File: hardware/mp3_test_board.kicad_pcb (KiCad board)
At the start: 2 copper layers, 113.1 x 53 mm, 128 parts, among them J1 874380343, J2 PJ-3270, J3 TF01-A, J4 532610371, P1 HRO-TYPE-C-31-M-12, SW1 TS-1010-C-A, SW2 TS-1157-X-F, SW3 TS-1157-X-F, SW4 TS-1157-X-F, SW5 TS-1157-X-F, SW6 TS-1157-X-F, SW7 TS-1010-C-A, SW8 TS-1010-C-A, U1 RT5750A, U10 OPA1652, U11 LM4562, U12 W25Q128JVSIQ, U13 XC6206P302MR, U2 RT9467, U3 RT4812, U4 F1C200S, U5 RT6150, U6 RT5750A, U7 RT5750A, U8 USBLC6-2SC6, U9 WM8741, Y1 Crystal_GND24

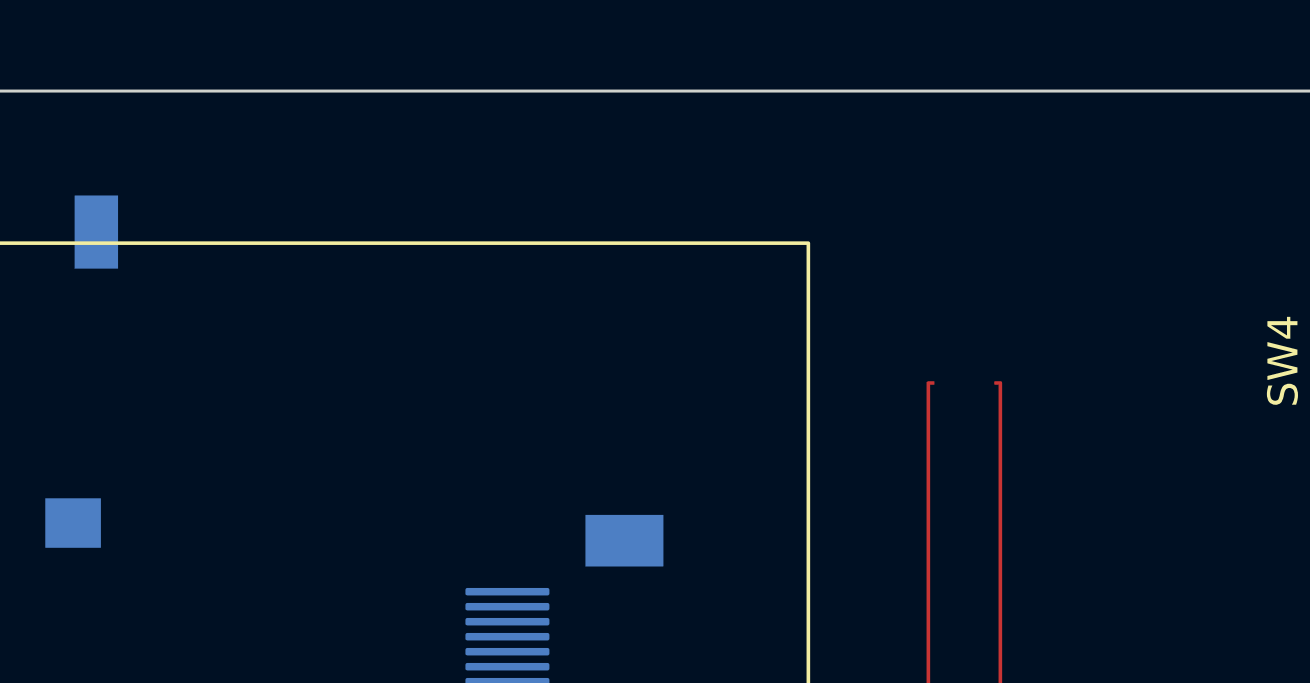
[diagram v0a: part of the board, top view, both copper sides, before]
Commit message: replaced dc-dc ics
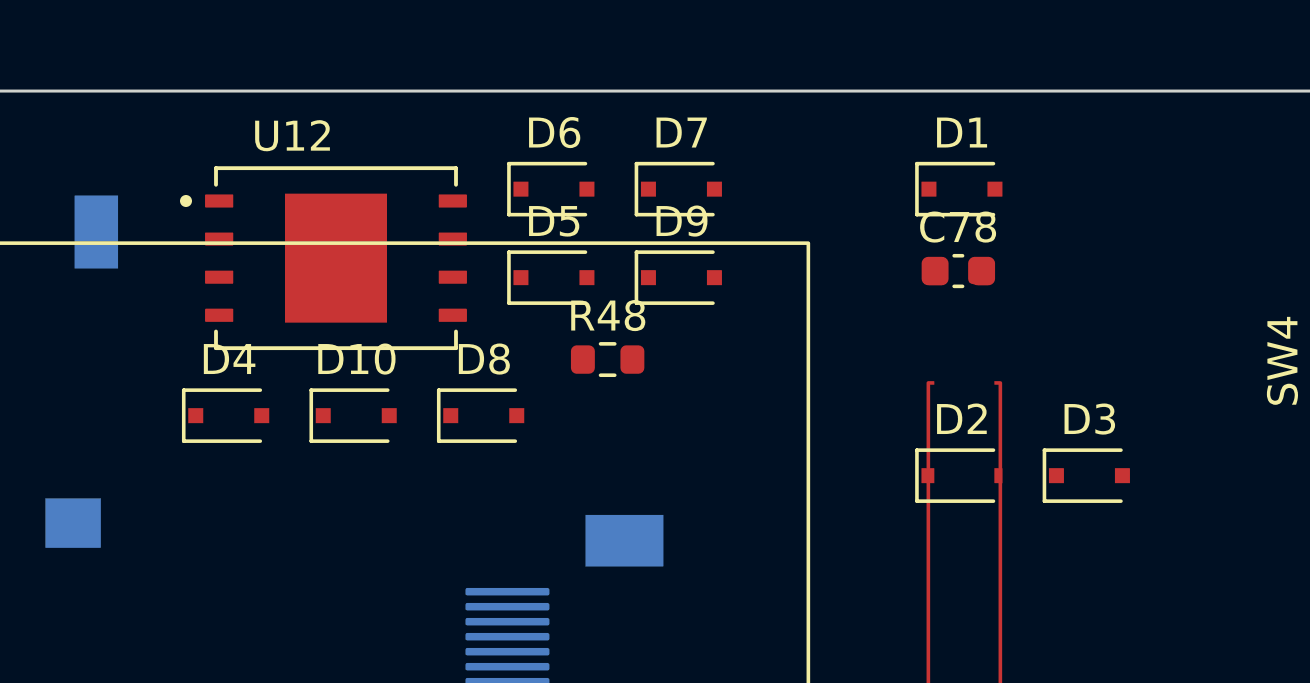
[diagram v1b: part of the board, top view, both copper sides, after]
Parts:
- added C78: C, rlib_passive:C_0603_1608Metric, F.Cu at (113.0, 64.0)
- added D1: PESD3V3L1BA, rlib_passive:D_SOD-323F, F.Cu at (113.1, 61.3)
- added D10: PESD3V3L1BA, rlib_passive:D_SOD-323F, F.Cu at (92.9, 68.8)
- added D2: PESD3V3L1BA, rlib_passive:D_SOD-323F, F.Cu at (113.1, 70.8)
- added D3: PESD3V3L1BA, rlib_passive:D_SOD-323F, F.Cu at (117.4, 70.8)
- added D4: PESD3V3L1BA, rlib_passive:D_SOD-323F, F.Cu at (88.7, 68.8)
- added D5: PESD3V3L1BA, rlib_passive:D_SOD-323F, F.Cu at (99.5, 64.2)
- added D6: PESD3V3L1BA, rlib_passive:D_SOD-323F, F.Cu at (99.5, 61.3)
- added D7: PESD3V3L1BA, rlib_passive:D_SOD-323F, F.Cu at (103.8, 61.3)
- added D8: PESD3V3L1BA, rlib_passive:D_SOD-323F, F.Cu at (97.2, 68.8)
- added D9: PESD3V3L1BA, rlib_passive:D_SOD-323F, F.Cu at (103.8, 64.2)
- added R48: R, rlib_passive:R_0603_1608Metric, F.Cu at (101.3, 67.0)
- added U12: MX25L25635F, rlib_ic:SON127P600X800X80-9N, F.Cu at (92.3, 63.6)
- R45: value R -> 10K
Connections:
- net CHRG_EN renamed /POWER/CHRG_EN
- net DAC_I2S_BCLK renamed /DAC/I2S_BCLK
- net DAC_I2S_DIN renamed /DAC/I2S_DIN
- net DAC_I2S_LRCK renamed /DAC/I2S_LRCK
- net SOC_I2C_SCL renamed /DAC/I2C_SCL
- net SOC_I2C_SDA renamed /DAC/I2C_SDIN
- J2 pad 6: unconnected-(J2-Pad6) -> /DAC/HP_PLUG
- JP3 pad 1: Net-(JP3-Pad1) -> /SOC/FLASH_SPI_CS
- U4 pad 37: unconnected-(U4-Pad37) -> /DAC/I2S_MCLK
- U4 pad 39: /SOC/FLASH_SPI_MISO -> unconnected-(U4-Pad39)
- U4 pad 40: /SOC/FLASH_SPI_CLK -> unconnected-(U4-Pad40)
- U4 pad 41: /SOC/FLASH_SPI_MOSI -> /SOC/CHR_IRQ
- U4 pad 42: /SOC/FLASH_SPI_CS -> /DAC/HP_PLUG
- U4 pad 59: CHRG_IRQ -> /SOC/FLASH_SPI_CLK
- U4 pad 60: Net-(JP3-Pad1) -> /SOC/FLASH_SPI_CS
- U4 pad 61: unconnected-(U4-Pad61) -> /SOC/FLASH_SPI_MISO
- U4 pad 62: AUDIO_PLUG -> /SOC/FLASH_SPI_MOSI
- U9 pad 5: DAC_I2S_MCLK -> /DAC/I2S_MCLK

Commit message: sfsf
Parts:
- added C106: 0.1u, rlib_passive:C_0603_1608Metric, F.Cu at (161.9, 119.1)
- added C107: 0.1u, rlib_passive:C_0603_1608Metric, F.Cu at (149.0, 132.0)
- added C110: 0.1u, rlib_passive:C_0603_1608Metric, F.Cu at (157.9, 121.6)
- added C111: 0.1u, rlib_passive:C_0603_1608Metric, F.Cu at (161.9, 121.6)
- added C82: 0.1u, rlib_passive:C_0603_1608Metric, F.Cu at (145.0, 132.0)
- added C83: 0.1u, rlib_passive:C_0603_1608Metric, F.Cu at (157.9, 119.1)
- added C92: 0.1u, rlib_passive:C_0603_1608Metric, F.Cu at (157.9, 124.1)
- added C93: 0.1u, rlib_passive:C_0603_1608Metric, F.Cu at (141.0, 132.0)
- added D11: SY8008B, rlib_power:SOT-23-5, F.Cu at (177.3, 120.1)
- added D12: SY8008B, rlib_power:SOT-23-5, F.Cu at (172.2, 120.1)
- added D13: SY8008B, rlib_power:SOT-23-5, F.Cu at (172.2, 124.5)
- added J1: PJ-322, rlib_connectors:PJ-322, B.Cu at (153.3, 72.0)
- added U14: OPA1656, rlib_ic:SOIC-8_3.9x4.9mm_P1.27mm, F.Cu at (151.7, 127.5)
- added U15: OPA1656, rlib_ic:SOIC-8_3.9x4.9mm_P1.27mm, F.Cu at (143.2, 127.5)
- added U6: LM4562, rlib_ic:SOIC-8_3.9x4.9mm_P1.27mm, F.Cu at (143.2, 121.1)
- added U7: LM4562, rlib_ic:SOIC-8_3.9x4.9mm_P1.27mm, F.Cu at (151.7, 121.1)
- C16, C17, C2: value C -> 10u
- R29, R3, R30, R31, R32, R33, R8: value R -> 10k
- SW1, SW7, SW8: footprint rlib_buttons:TS-1010-X-X -> rlib_buttons:GT-TC054A-H035-L1
- SW2, SW3, SW4, SW5, SW6: value TS-1157-X-F -> K2-1156SP-F5SW-05; footprint rlib_buttons:TS-1157-X-F -> rlib_buttons:K2-1156SP-F5SW-05
- U12: moved to B.Cu
- moved REF** 77.4 mm to (44.0, 62.2), turned to -90 degrees
- moved J2 40.2 mm to (193.0, 76.0)
- moved SW7 9.48 mm to (79.8, 109.6)
- moved SW8 9.44 mm to (69.0, 109.3)
- moved SW1 9.40 mm to (57.2, 109.4)
- moved SW3 7.21 mm to (122.8, 97.0)
- moved SW4 6.25 mm to (123.0, 69.0)
- moved D3 6.00 mm to (111.4, 70.8)
- moved SW2 6.00 mm to (123.0, 83.0)
- moved SW5 6.00 mm to (114.0, 83.0)
- moved SW6 6.00 mm to (132.0, 83.0)
- moved U10 6.00 mm to (128.0, 77.0)
- moved U11 6.00 mm to (128.0, 94.0)
- moved U9 6.00 mm to (117.0, 84.0)
- moved U12 2.73 mm to (91.0, 66.0), turned to 180 degrees
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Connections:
- R6 pad 2: Net-(R6-Pad2) -> Net-(D11-Pad5)
- R7 pad 1: Net-(R6-Pad2) -> Net-(D11-Pad5)
- U2 pad 5: /DAC/I2C_SCL -> /NewDAC/I2C_SDIN
- U2 pad 6: /DAC/I2C_SDIN -> /NewDAC/I2C_SCL
- U4 pad 23: /DAC/I2C_SCL -> /NewDAC/I2C_SDIN
- U4 pad 24: /DAC/I2C_SDIN -> /NewDAC/I2C_SCL
- U4 pad 37: /DAC/I2S_MCLK -> /NewDAC/I2S_MCLK
- U4 pad 42: /DAC/HP_PLUG -> /SOC/HP_PLUG
- U4 pad 63: /DAC/I2S_DIN -> /NewDAC/I2S_DIN
- U4 pad 65: /DAC/I2S_LRCK -> /NewDAC/I2S_LRCK
- U4 pad 66: /DAC/I2S_BCLK -> /NewDAC/I2S_BCLK

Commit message: added new power list
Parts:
- removed C26, C28, C30, C32, C37, C38, C45, C46: 0.1u, rlib_passive:C_0603_1608Metric
- removed C33, C34: 3.3n, rlib_passive:C_0603_1608Metric
- removed D2, D3: PESD3V3L1BA, rlib_passive:D_SOD-323F
- removed the J1 at (262.4, 93.2)
- removed the J1 at (153.3, 72.0)
- removed J2: PJ-3270, rlib_connectors:PJ-3270
- removed R42, R48: R, rlib_passive:R_0603_1608Metric
- removed R45: 10K, rlib_passive:R_0603_1608Metric
- removed the REF** at (44.0, 62.2)
- removed the REF** at (148.0, 62.0)
- removed the REF** at (149.0, 107.0)
- removed the REF** at (44.0, 107.0)
- removed the REF** at (44.3, 61.5)
- removed U1: RT5750A, rlib_power:SOT-23-5
- removed U10: OPA1652, rlib_ic:SOIC-8_3.9x4.9mm_P1.27mm
- removed U11: LM4562, rlib_ic:SOIC-8_3.9x4.9mm_P1.27mm
- removed the U12 at (91.0, 66.0)
- removed the U12 at (72.0, 91.0)
- removed the U6 at (143.2, 121.1)
- removed the U6 at (294.4, 109.0)
- removed the U7 at (151.7, 121.1)
- removed the U7 at (296.3, 123.1)
- removed U9: WM8741, rlib_ic:SSOP-28_5.3x10.2mm_P0.65mm
- added ?: , , F.Cu at (185.0, 112.0)
- added ?: , , F.Cu at (185.0, 65.0)
- added J1: PJ-322, rlib_connectors:PJ-322, B.Cu at (189.3, 74.0)
- added REF**: MountingHole_3.2mm_M3_DIN965_Pad, MountingHole:MountingHole_3.2mm_M3_DIN965_Pad, F.Cu at (83.0, 64.0)
- added REF**: MountingHole_3.2mm_M3_DIN965_Pad, MountingHole:MountingHole_3.2mm_M3_DIN965_Pad, F.Cu at (83.0, 112.0)
- added REF**: WF24LTYAJDNN0, rlib_lcd:WF24LTYAJDNN0_копия, F.Cu at (85.0, 66.6)
- added U12: MX25L25635F, rlib_ic:SON127P600X800X80-9N, F.Cu at (125.0, 158.0)
- added U6: LM4562, rlib_ic:SOIC-8_3.9x4.9mm_P1.27mm, F.Cu at (183.4, 135.8)
- added U7: LM4562, rlib_ic:SOIC-8_3.9x4.9mm_P1.27mm, F.Cu at (208.6, 126.9)
- J4, U13, U2, U4, U5: moved to F.Cu
- moved R2 196.6 mm to (119.2, 187.4)
- moved U3 187.2 mm to (115.5, 181.5)
- moved R10 186.9 mm to (131.2, 186.6)
- moved R1 186.2 mm to (123.2, 184.8)
- moved R4 182.2 mm to (131.2, 184.1)
- moved R12 179.4 mm to (133.0, 178.4)
- moved R7 179.1 mm to (125.0, 177.8)
- moved R29 178.9 mm to (129.5, 139.8)
- moved R41 176.9 mm to (132.2, 158.0)
- moved R32 175.4 mm to (136.8, 153.0)
- moved R5 175.1 mm to (132.5, 173.4)
- moved R34 175.0 mm to (141.1, 150.1)
- moved R9 174.8 mm to (132.1, 181.6)
- moved R37 171.2 mm to (136.4, 155.5)
- moved R31 170.4 mm to (136.2, 158.1)
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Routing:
- net GND: track 45.8 -> 0.00 mm
- removed copper zone on F.Cu, net /SOC/LCD_D10
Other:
- board size 113.1 x 53 mm -> 110 x 56 mm

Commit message: some changes
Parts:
- removed ? (x2): , 
- removed C1, C18, C19, C21, C22, C3, C4, C5, C51, C52, C53, C76, C77, C78: C, rlib_passive:C_0603_1608Metric
- removed C16, C2: 10u, rlib_passive:C_0603_1608Metric
- removed C69: 100n, rlib_passive:C_0603_1608Metric
- removed D11, D12, D13: SY8008B, rlib_power:SOT-23-5
- removed J4: 532610371, rlib_connectors:MOLEX_532610371
- removed R1, R10, R13, R14, R2, R4, R41, R5, R6, R7, R9: R, rlib_passive:R_0603_1608Metric
- removed REF** (x2): MountingHole_3.2mm_M3_DIN965_Pad, MountingHole:MountingHole_3.2mm_M3_DIN965_Pad
- removed REF**: WF24LTYAJDNN0, rlib_lcd:WF24LTYAJDNN0_копия
- removed U13: XC6206P302MR, rlib_power:SOT-23
- added C104: 10u, rlib_passive:T491A106K010AT, F.Cu at (52.7, 90.9)
- added C105: 10u, rlib_passive:T491A106K010AT, F.Cu at (48.0, 90.9)
- added C108: 10u, rlib_passive:T491A106K010AT, F.Cu at (52.7, 94.2)
- added C109: 10u, rlib_passive:T491A106K010AT, F.Cu at (57.4, 87.6)
- added C80: 10u, rlib_passive:T491A106K010AT, F.Cu at (57.4, 84.2)
- added C81: 10u, rlib_passive:T491A106K010AT, F.Cu at (66.8, 84.2)
- added C84: 10u, rlib_passive:T491A106K010AT, F.Cu at (62.1, 87.6)
- added C85: 10u, rlib_passive:T491A106K010AT, F.Cu at (48.0, 94.2)
- added C86: 10u, rlib_passive:T491A106K010AT, F.Cu at (48.0, 87.6)
- added C87: 10u, rlib_passive:T491A106K010AT, F.Cu at (48.0, 84.2)
- added C88: 10u, rlib_passive:T491A106K010AT, F.Cu at (62.1, 84.2)
- added C89: 10u, rlib_passive:T491A106K010AT, F.Cu at (72.1, 94.5)
- added C90: 10u, rlib_passive:T491A106K010AT, F.Cu at (52.7, 84.2)
- added C91: 10u, rlib_passive:T491A106K010AT, F.Cu at (52.7, 87.6)
- added D2: HCTL HC-1.25-3PWT, rlib_connectors:CONN-SMD_HC-1.25-3PWT, B.Cu at (170.7, 109.7)
- added D3: PESD3V3L1BA, rlib_passive:D_SOD-323F, F.Cu at (138.7, 96.0)
- added L1: 4.7u, rlib_passive:IND_LQH32PN4R7NN0L, F.Cu at (30.0, 10.2)
- added L10: L, rlib_passive:INDC2520X120N, F.Cu at (29.5, 13.2)
- added L11: L, rlib_passive:INDC2520X120N, F.Cu at (1.98, 25.0)
- added L12: L, rlib_passive:INDC2520X120N, F.Cu at (1.98, 21.2)
- added L13: L, rlib_passive:INDC2520X120N, F.Cu at (6.94, 25.0)
- added L2: 4.7u, rlib_passive:IND_LQH32PN4R7NN0L, F.Cu at (21.8, 5.83)
- added L3: 4.7u, rlib_passive:IND_LQH32PN4R7NN0L, B.Cu at (101.1, 63.5)
- added L4: 4.7u, rlib_passive:IND_LQH32PN4R7NN0L, F.Cu at (24.4, 20.8)
- added L5: 2.2u, rlib_passive:IND_LQH32PN4R7NN0L, F.Cu at (130.0, 112.3)
- added L6: 2.2u, rlib_passive:IND_LQH32PN4R7NN0L, F.Cu at (125.1, 112.3)
- added L9: L, rlib_passive:INDC2520X120N, F.Cu at (35.0, 1.38)
- added P2: WF24LTYAJDNN0#, rlib_lcd:WF24LTYAJDNN0, F.Cu at (144.6, 109.0)
- C10, C11, C12, C13, C14, C20, C6, C7, C8, C9: value C -> 10u; footprint rlib_passive:C_0603_1608Metric -> rlib_passive:T491A106K010AT
- C17: footprint rlib_passive:C_0603_1608Metric -> rlib_passive:T491A106K010AT
- D1: value PESD3V3L1BA -> HCTL HC-1.25-3PWT; footprint rlib_passive:D_SOD-323F -> rlib_connectors:CONN-SMD_HC-1.25-3PWT
- R11, R12, R34, R35, R36, R37, R39, R46, R47: value R -> 10k
- R40: value R -> 100
- R43, R44: value R -> 27
- SW1: value TS-1010-C-A -> K2-1156SP-F5SW-05; footprint rlib_buttons:GT-TC054A-H035-L1 -> rlib_buttons:K2-1156SP-F5SW-05
- SW7, SW8: value TS-1010-C-A -> GT-TC054A-H035-L1
- U12, U14, U15, U4, U6, U7: moved to B.Cu
- U2: value RT9467 -> AXP192; footprint rlib_power:WQFN-24-1EP_4x4mm_P0.5mm_EP2.45x2.45mm -> rlib_power:QFN-48-1EP_6x6mm_P0.4mm_EP4.66x4.66mm; moved to B.Cu
- U3: value RT4812 -> SGM6603-ADJYN6G; footprint rlib_power:TSOT-23-8 -> rlib_power:SOT-23-6
- U5: value RT6150 -> SGM3204; footprint rlib_power:RT6150AGQW -> rlib_power:SOT-23-6
- Y1: value Crystal_GND24 -> XRCGB24M000F1H01R0; footprint rlib_crystals:Crystal_SMD_Abracon_ABM8G-4Pin_3.2x2.5mm -> rlib_crystals:OSC_XRCGB24M000F1H01R0
- moved U3 202.6 mm to (21.9, 1.73)
- moved U5 198.7 mm to (12.7, 9.97)
- moved D1 143.1 mm to (63.0, 51.8)
- moved C20 114.6 mm to (48.0, 103.9)
- moved C17 112.8 mm to (48.0, 100.6)
- moved C10 112.1 mm to (57.4, 103.9)
- moved C8 111.2 mm to (52.7, 103.9)
- moved R12 110.9 mm to (75.9, 83.3)
- moved C14 110.7 mm to (52.7, 107.2)
- moved C11 109.4 mm to (48.0, 107.2)
- moved C12 106.7 mm to (52.7, 100.6)
- moved C9 106.2 mm to (57.4, 107.2)
- moved C6 103.0 mm to (57.4, 100.6)
- moved C13 99.0 mm to (62.1, 100.6)
- moved C7 94.8 mm to (62.1, 103.9)
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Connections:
- net Net-(C69-Pad1) renamed /SOC/RESET
- C10 pad 1: Net-(C10-Pad1) -> +2V5
- C11 pad 1: Net-(C11-Pad1) -> +3V3
- C11 pad 2: Net-(C11-Pad2) -> GND
- C12 pad 1: +5VA -> +1V1
- C12 pad 2: GNDA -> GND
- C13 pad 1: GNDA -> VCC
- C13 pad 2: -5VA -> GND
- C14 pad 1: +BATT -> +5VA
- C17 pad 1: VCC -> Net-(C17-Pad1)
- C20 pad 1: +2V5 -> +5VA
- C55 pad 2: GND -> Net-(C55-Pad2)
- C58 pad 2: GND -> Net-(C55-Pad2)
- C6 pad 1: Net-(C6-Pad1) -> VCC
- C7 pad 1: Net-(C6-Pad1) -> VCC
- C8 pad 1: Net-(C8-Pad1) -> VCC
- C8 pad 2: GNDA -> GND
- C9 pad 1: GNDA -> VCC
- C9 pad 2: Net-(C4-Pad2) -> GND
- D1 pad 1: GND -> unconnected-(D1-Pad1)
- D1 pad 2: PWR_BTN -> unconnected-(D1-Pad2)
- J1 pad 3: unconnected-(J1-Pad3) -> GNDA
- J3 pad 9: unconnected-(J3-Pad9) -> SD_PLUG
- R11 pad 1: +1V1 -> Net-(P2-Pad30)
- R11 pad 2: Net-(C19-Pad2) -> +3V3
- R12 pad 1: Net-(C19-Pad2) -> SD_PLUG
- R12 pad 2: GND -> +3V3
- SW1 pad 1: PWR_BTN -> GND
- SW1 pad 3: (no net) -> Net-(U2-Pad23)
- SW1 pad 4: (no net) -> Net-(U2-Pad23)
- U2 pad 1: VBUS -> /NewDAC/I2C_SCL
- U2 pad 10: Net-(R1-Pad2) -> +1V1
- U2 pad 12: PWR_BTN -> unconnected-(U2-Pad12)
- U2 pad 13: +BATT -> Net-(R7-Pad1)
- U2 pad 14: +BATT -> VCC
- U2 pad 15: VCC -> Net-(L1-Pad1)
- U2 pad 16: VCC -> GND
- U2 pad 17: GND -> +2V5
- U2 pad 18: GND -> unconnected-(U2-Pad18)
- U2 pad 19: Net-(C11-Pad2) -> unconnected-(U2-Pad19)
- U2 pad 2: unconnected-(U2-Pad2) -> /NewDAC/I2C_SDIN
- U2 pad 20: Net-(C11-Pad2) -> unconnected-(U2-Pad20)
- U2 pad 21: Net-(C11-Pad1) -> Net-(C1-Pad1)
- U2 pad 22: Net-(C10-Pad1) -> GND
- U2 pad 23: Net-(C6-Pad1) -> Net-(U2-Pad23)
- U2 pad 24: unconnected-(U2-Pad24) -> Net-(R5-Pad2)
- U2 pad 25: GND -> Net-(C4-Pad1)
- U2 pad 3: unconnected-(U2-Pad3) -> Net-(U2-Pad3)
- U2 pad 5: /NewDAC/I2C_SDIN -> /NewPower2/RESET
- U2 pad 6: /NewDAC/I2C_SCL -> unconnected-(U2-Pad6)
- U2 pad 7: CHRG_IRQ -> VCC
- U2 pad 8: unconnected-(U2-Pad8) -> Net-(L3-Pad1)
- U2 pad 9: /POWER/CHRG_EN -> GND
- U3 pad 2: Net-(R4-Pad2) -> GND
- U3 pad 3: Net-(C8-Pad1) -> VCC
- U3 pad 4: GNDA -> Net-(R10-Pad2)
- U3 pad 5: GNDA -> Net-(C17-Pad1)
- U4 pad 40: unconnected-(U4-Pad40) -> SD_PLUG
- U4 pad 41: /SOC/CHR_IRQ -> /NewPower2/IRQ
- U5 pad 1: +3V3 -> Net-(C18-Pad1)
- U5 pad 2: Net-(L5-Pad2) -> +5VA
- U5 pad 3: GND -> Net-(C16-Pad2)
- U5 pad 4: Net-(L5-Pad1) -> GND
- U5 pad 5: +BATT -> +5VA
- U5 pad 6: unconnected-(U5-Pad6) -> Net-(C16-Pad1)
- Y1 pad 2: GND -> (no net)
- Y1 pad 4: GND -> (no net)
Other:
- outline, holes or cut-outs redrawn
